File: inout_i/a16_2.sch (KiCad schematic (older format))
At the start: 30 parts, among them U16021 74LVC07, U16030 74HC04, U16031 74HC02, U16032 74HC27, U16033 74HC02, U16034 74HC02, U16035 74HC02, U16036 74HC02, U16037 74HC02, U16038 74HC04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

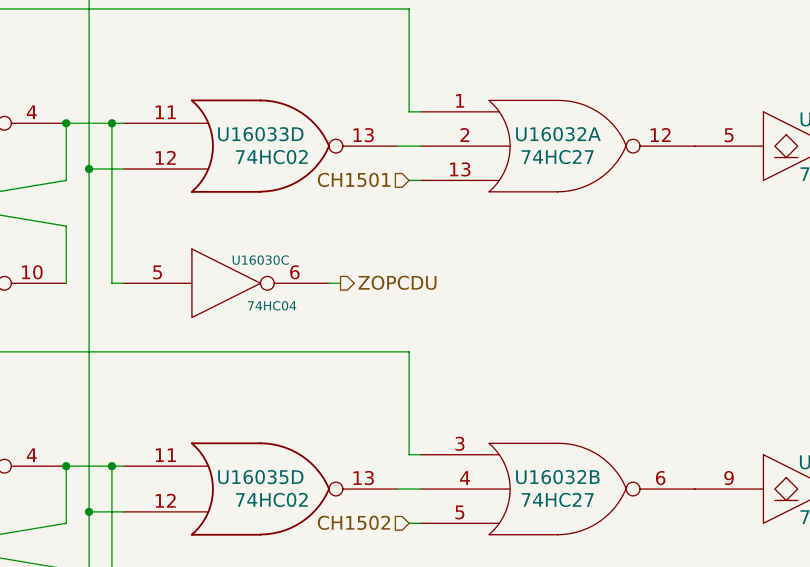
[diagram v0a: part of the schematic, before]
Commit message: Broke out most (all?) of the DSKY outputs
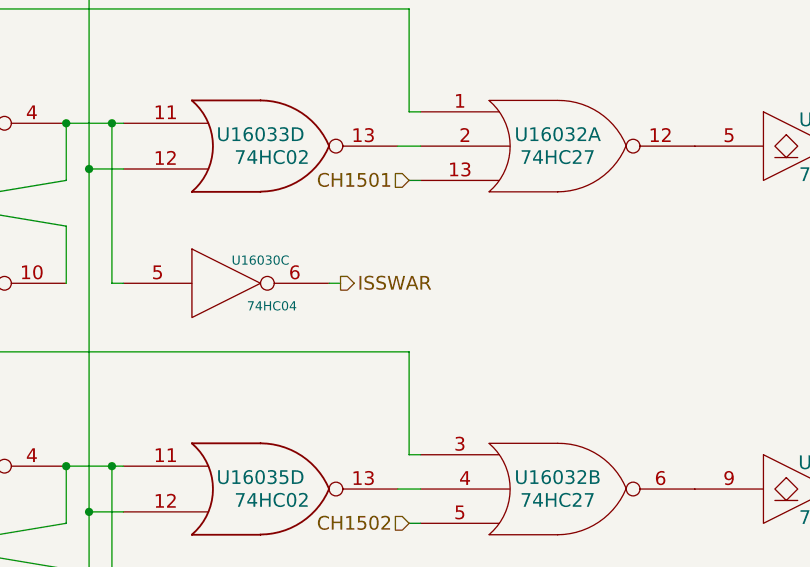
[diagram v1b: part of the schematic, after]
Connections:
- net ZOPCDU: no longer U16030.6
- new net ISSWAR: U16030.6
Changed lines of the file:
@@
 $EndComp
 Text HLabel 14250 4000 2    60   Output ~ 0
-ZOPCDU
+ISSWAR
 $Comp
 L 74HC27 U16032

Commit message: Fixed not->1-input nor in the rest of the modules.
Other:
- moved on the sheet: U16030B, U16030C, U16030D, U16030E, U16030F, U16038A, U16038B, U16038C, U16038D, U16038E, U16038F, U16047D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
